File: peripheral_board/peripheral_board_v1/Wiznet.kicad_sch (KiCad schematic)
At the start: 34 parts, among them SW3 3_Pin_Dip_Switch_DSWB03LHGET_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, U4 W5500, U5 SN74AHC1G125DBVR, Y2 25MHz

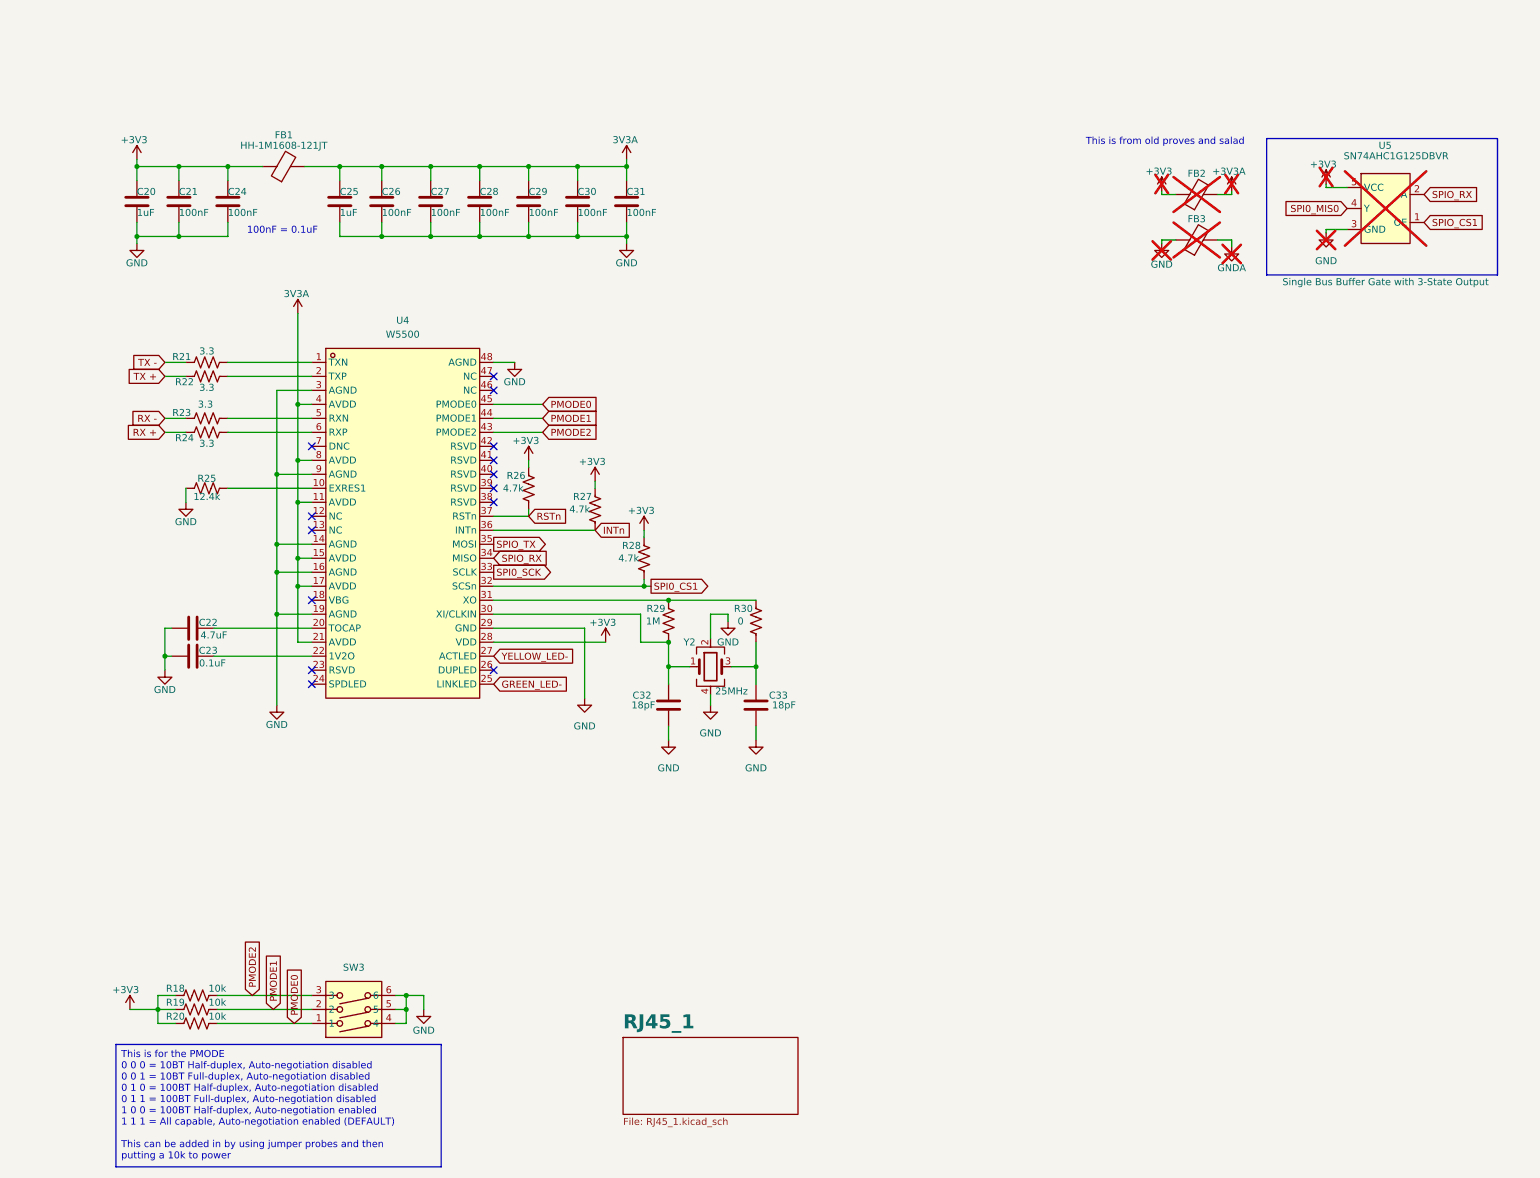
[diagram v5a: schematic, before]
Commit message: Started the PCB layout
Finished the schematic. Now working on the PCB. Might looking in to moving to a 6 layer board.
Need to do a bit of redesign because changing some of the parts had different footprints.

Started on the Wiznet and the its RJ45 port it has. Want to make the port close to the chip as a possible. Currently working on the 4 layer stack up but if I switch to a 6 layer it might help with impedance and change the overall signal layering.
Almost done with the Wiznet just need to do the clock and the TX/RX pairs.
Once that is done I will work on the Ethernet switch then lastly the breakout pins for the RP.

I should have selected either a 6 layer or 4 layer board, leaning more towards 6 layer because I can keep my signals separated by the 3 and 3 sections.
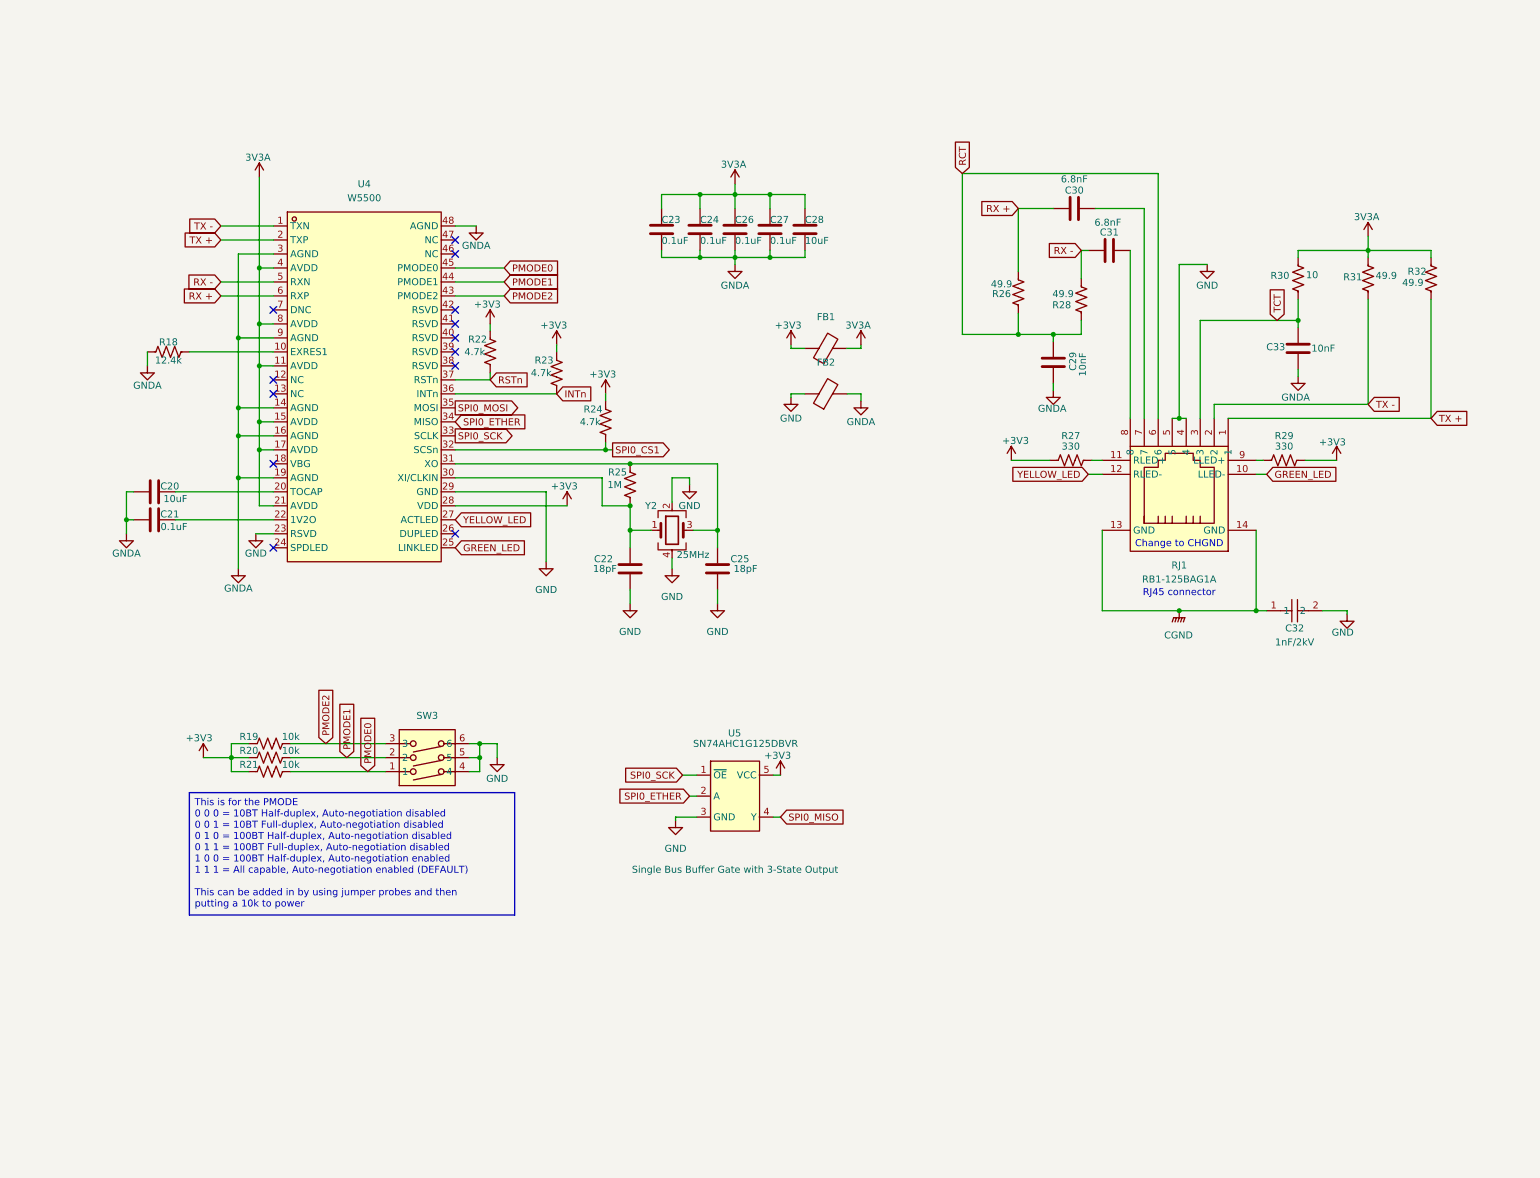
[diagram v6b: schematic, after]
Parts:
- removed C20, C25: 1uF, Capacitor_SMD:C_0402_1005Metric, symbol Device:C
- removed C21: 100nF, Capacitor_SMD:C_0402_1005Metric, symbol Device:C
- removed FB3: FerriteBead, symbol Device:FerriteBead
- removed R21, R22, R23, R24: 3.3, symbol Device:R_US
- added C23: 0.1uF, Capacitor_SMD:C_0402_1005Metric, symbol Device:C
- added C32: 1nF/2kV, SCALES:C1210, symbol SCALES:FV32N102J202EFG
- added C33: 10nF, Capacitor_SMD:C_0402_1005Metric, symbol Device:C
- added R26, R28, R31, R32: 49.9, Resistor_SMD:R_0603_1608Metric, symbol Device:R_US
- added R27, R29: 330, Resistor_SMD:R_0603_1608Metric, symbol Device:R_US
- added RJ1: RB1-125BAG1A, easyeda2kicad:RJ45-TH_RB1-125BAG1A, symbol easyeda2kicad:RB1-125BAG1A
- C20: renamed from C22; value 4.7uF -> 10uF
- C24, C26, C27: value 100nF -> 0.1uF
- C28: value 100nF -> 10uF
- C29: value 100nF -> 10nF
- C30, C31: value 100nF -> 6.8nF
- FB2: value FerriteBead -> HH-1M1608-121JT; footprint (none) -> Inductor_SMD:L_0603_1608Metric; now fitted; now in the parts list
- R30: value 0 -> 10
- U4: footprint easyeda2kicad:LQFP-48_L7.0-W7.0-P0.50-LS9.0-BL -> SCALES:LQFP-48_L7.0-W7.0-P0.50-LS9.0-BL
- U5: now fitted; now in the parts list
- renumbered C23 to C21, C32 to C22, C33 to C25, R25 to R18, R18 to R19, R19 to R20, R20 to R21, R26 to R22, R27 to R23, R28 to R24, R29 to R25
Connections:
- net +3V3A is gone; now on net GNDA: FB2.2
- net SPIO_CS1 is gone; now on net SPI0_SCK: U5.1 (~{OE})
- net +3V3: now also R27.2, R29.1; no longer C24.2, FB2.1
- net 3V3A: now also C24.2, R30.2, C23.2, R31.2, R32.2; no longer C29.2, C30.2, C31.2
- net GND: now also FB2.1, U4.23 (RSVD), C32.2, RJ1.4, RJ1.5; no longer C20.2, C21.2, C24.1, C26.1, C27.1, C28.1, C29.1, C30.1, C31.1, R18.1, U4.14 (AGND), U4.16 (AGND), U4.19 (AGND), U4.3 (AGND), U4.48 (AGND), U4.9 (AGND)
- net GNDA: now also C20.2, C21.2, C24.1, C26.1, C27.1, C28.1, C29.1, R18.1, U4.14 (AGND), U4.16 (AGND), U4.19 (AGND), U4.3 (AGND), U4.48 (AGND), U4.9 (AGND), C23.1, C33.1
- net RX +: now also C30.1, U4.6 (RXP), R26.2
- net RX -: now also C31.1, U4.5 (RXN), R28.2
- net TX +: now also U4.2 (TXP), R32.1, RJ1.1
- net TX -: now also U4.1 (TXN), R31.1, RJ1.2
- net at C25.2, Y2.3: now also R25.2, U4.31 (XO); no longer R30.1
- net GREEN_LED- renamed GREEN_LED
- net GREEN_LED: now also RJ1.10 (LLED-)
- net SPI0_MIS0 renamed SPI0_MISO
- net SPIO_RX renamed SPI0_ETHER
- net SPIO_TX renamed SPI0_MOSI
- net YELLOW_LED- renamed YELLOW_LED
- net YELLOW_LED: now also RJ1.12 (RLED-)
- new net: R29.2, RJ1.9 (LLED+)
- new net: R27.1, RJ1.11 (RLED+)
- new net: C30.2, RJ1.7
- new net: C31.2, RJ1.8
- new net CGND: C32.1, RJ1.13 (GND), RJ1.14 (GND)
- new net RCT: C29.2, R26.1, R28.1, RJ1.6
- new net TCT: C33.2, R30.1, RJ1.3
- no-connect marks 14 -> 13
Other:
- removed sheet RJ45_1
- note added: "Change to CHGND"
- note added: "RJ45 connector"
- note removed: "100nF = 0.1uF"
- note removed: "This is from old proves and salad"
- moved on the sheet: C20, C21, C22, C25, FB1, R18, R19, R20, R21, R22, R23, R24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
